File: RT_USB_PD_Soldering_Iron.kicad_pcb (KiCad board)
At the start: 4 copper layers, 75 x 11 mm, 62 parts, among them J1 USB4105-GF-A, J2 35RASMT4BHNTRX, J3 Conn_02x03_Odd_Even, SW1 SW_Push, SW2 SW_Push, U1 SPX3819M5-L-3-3, U2 BMI270, U3 DRTR5V0U4S-7, U5 STM32G431Kxxx, U6 TPS25982ONRGET, U7 OPA376AIDCKR, U8 STTS22H, Y1 NX2016SA-24MHZ-EXS00A-CS10820

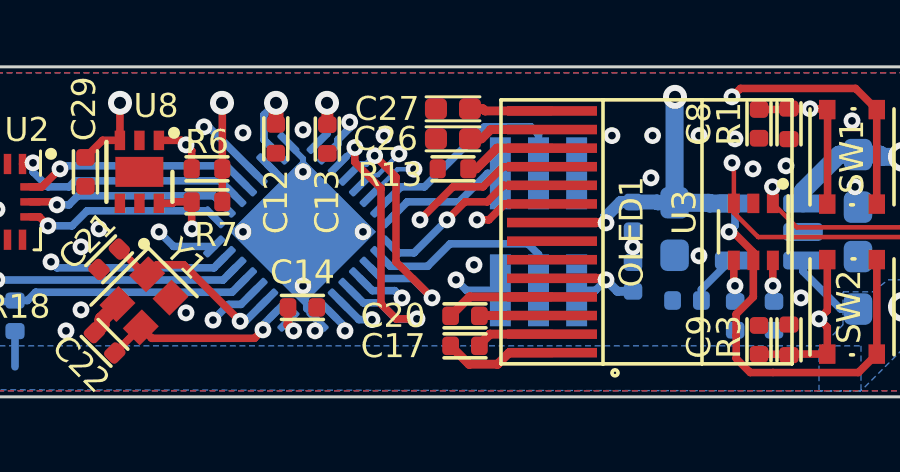
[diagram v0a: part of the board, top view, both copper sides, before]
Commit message: slight change in capacitor layout
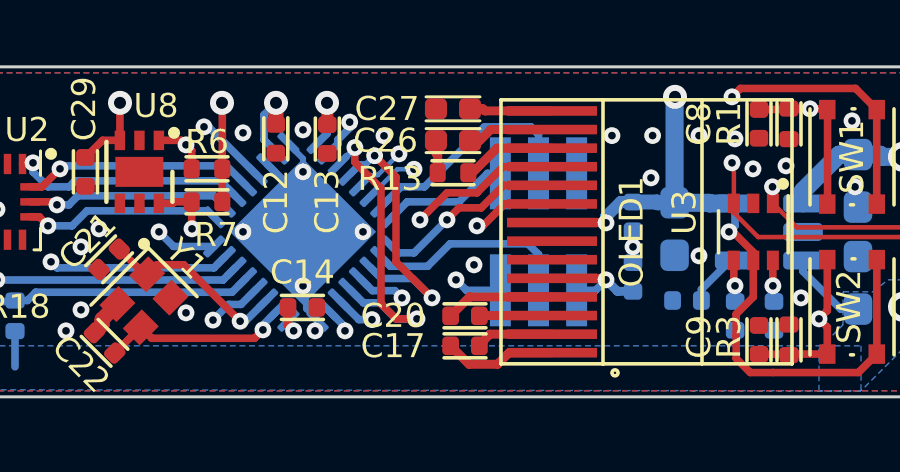
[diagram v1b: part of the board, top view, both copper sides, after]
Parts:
- moved R13 0.13 mm to (152.2, 123.0)
- moved C26 0.06 mm to (152.2, 122.0)
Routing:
- net GND: track 17.2 -> 18.3 mm
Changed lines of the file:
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@@
   )
   (module "local:C_0402_1005Metric_Pad0.74x0.62mm_HandSolder" (layer "F.Cu")
-    (at 152.2 121.9)
+    (at 152.2 121.958771)
     (descr "Capacitor SMD 0402 (1005 Metric), square (rectangular) end terminal, IPC_7351 nominal with elongated pad for handsoldering. (Body size source: IPC-SM-782 page 76, https://www.pcb-3d.com/wordpress/wp-content/uploads/ipc-sm-782a_amendment_1_and_2.pdf), generated with kicad-footprint-generator")
     (tags "capacitor handsolder")
@@
   )
   (module "local:R_0402_1005Metric" (layer "F.Cu")
-    (at 152.2 122.9)
+    (at 152.2 123.029328)
     (descr "Resistor SMD 0402 (1005 Metric), square (rectangular) end terminal, IPC_7351 nominal, (Body size source: IPC-SM-782 page 72, https://www.pcb-3d.com/wordpress/wp-content/uploads/ipc-sm-782a_amendment_1_and_2.pdf), generated with kicad-footprint-generator")
     (tags "resistor")
@@
   (segment (start 127.6 123.8) (end 127.2 124.2) (width 0.254) (layer "F.Cu") (net 15))
   (segment (start 126.85 124.95) (end 126.325 124.95) (width 0.254) (layer "F.Cu") (net 15))
-  (segment (start 153.15 121.9) (end 153.46 121.59) (width 0.3) (layer "F.Cu") (net 16))
-  (segment (start 153.46 121.59) (end 155.5 121.59) (width 0.3) (layer "F.Cu") (net 16))
-  (segment (start 153.15 121.9) (end 152.7675 121.9) (width 0.3) (layer "F.Cu") (net 16))
+  (segment (start 155.5 121.59) (end 153.46 121.59) (width 0.3) (layer "F.Cu") (net 16))
+  (segment (start 153.091229 121.958771) (end 152.7675 121.958771) (width 0.3) (layer "F.Cu") (net 16))
+  (segment (start 153.46 121.59) (end 153.091229 121.958771) (width 0.3) (layer "F.Cu") (net 16))
   (segment (start 153.2 120.9) (end 152.7675 120.9) (width 0.3) (layer "F.Cu") (net 17))
   (segment (start 155.5 120.97) (end 153.27 120.97) (width 0.3) (layer "F.Cu") (net 17))
@@
   (segment (start 131.3 120.9) (end 106.55 120.9) (width 0.4) (layer "In1.Cu") (net 22))
   (segment (start 105.35 120.9) (end 106.55 120.9) (width 0.4) (layer "B.Cu") (net 22))
-  (segment (start 152.98 122.9) (end 153.67 122.21) (width 0.3) (layer "F.Cu") (net 23))
+  (segment (start 152.850672 123.029328) (end 153.67 122.21) (width 0.3) (layer "F.Cu") (net 23))
   (segment (start 153.67 122.21) (end 155.5 122.21) (width 0.3) (layer "F.Cu") (net 23))
-  (segment (start 152.71 122.9) (end 152.98 122.9) (width 0.3) (layer "F.Cu") (net 23))
+  (segment (start 152.71 123.029328) (end 152.850672 123.029328) (width 0.3) (layer "F.Cu") (net 23))
   (segment (start 161.590953 125.954086) (end 161.445914 125.954086) (width 0.254) (layer "B.Cu") (net 24))
   (segment (start 161.445914 125.954086) (end 160.47954 126.92046) (width 0.254) (layer "B.Cu") (net 24))
@@
   (segment (start 125.85 123.95) (end 126.325 123.95) (width 0.254) (layer "F.Cu") (net 25))
   (segment (start 136.0875 124) (end 134.936877 124) (width 0.254) (layer "F.Cu") (net 25))
+  (segment (start 151.6325 121.958771) (end 151.6325 122.3825) (width 0.3) (layer "F.Cu") (net 25))
   (segment (start 126.325 124.45) (end 125.45 124.45) (width 0.254) (layer "F.Cu") (net 25))
+  (segment (start 151.6325 122.3825) (end 151.69 122.44) (width 0.3) (layer "F.Cu") (net 25))
   (segment (start 140.24659 128.360589) (end 140.5 128.107179) (width 0.5) (layer "F.Cu") (net 25))
   (segment (start 124.65 126.880201) (end 125.3 126.230201) (width 0.254) (layer "F.Cu") (net 25))
@@
   (segment (start 125.5 124.3) (end 125.85 123.95) (width 0.254) (layer "F.Cu") (net 25))
   (segment (start 140.5 127.922183) (end 141.016117 127.406066) (width 0.5) (layer "F.Cu") (net 25))
+  (segment (start 151.69 122.44) (end 151.69 123.029328) (width 0.3) (layer "F.Cu") (net 25))
   (segment (start 135.8 124.5) (end 135.7 124.6) (width 0.254) (layer "F.Cu") (net 25))
   (via (at 135.75 128.3) (size 0.56) (drill 0.254) (layers "F.Cu" "B.Cu") (remove_unused_layers) (keep_end_layers) (net 25))
@@
   (segment (start 147.2 122.560482) (end 147.2 123) (width 0.2032) (layer "B.Cu") (net 25))
   (segment (start 146.713864 122.03899) (end 146.713864 122.074346) (width 0.2032) (layer "B.Cu") (net 25))
-  (segment (start 153.890817 123.45) (end 153.340817 124) (width 0.254) (layer "F.Cu") (net 26))
+  (segment (start 153.890817 123.45) (end 153.140817 124.2) (width 0.254) (layer "F.Cu") (net 26))
   (segment (start 143.49 122.29) (end 143.3 122.1) (width 0.254) (layer "F.Cu") (net 26))
   (segment (start 155.5 123.45) (end 153.890817 123.45) (width 0.254) (layer "F.Cu") (net 26))
+  (segment (start 152.4 124.2) (end 152 124.6) (width 0.254) (layer "F.Cu") (net 26))
   (segment (start 142.397498 121.95) (end 143.15 121.95) (width 0.254) (layer "F.Cu") (net 26))
-  (segment (start 153.340817 124) (end 152.6 124) (width 0.254) (layer "F.Cu") (net 26))
   (segment (start 143.15 121.95) (end 143.3 122.1) (width 0.254) (layer "F.Cu") (net 26))
-  (segment (start 152.6 124) (end 152 124.6) (width 0.254) (layer "F.Cu") (net 26))
   (segment (start 143.49 122.9) (end 143.49 122.29) (width 0.254) (layer "F.Cu") (net 26))
+  (segment (start 153.140817 124.2) (end 152.4 124.2) (width 0.254) (layer "F.Cu") (net 26))
   (via (at 152 124.6) (size 0.56) (drill 0.254) (layers "F.Cu" "B.Cu") (remove_unused_layers) (keep_end_layers) (net 26))
   (via (at 143.3 122.1) (size 0.56) (drill 0.254) (layers "F.Cu" "B.Cu") (remove_unused_layers) (keep_end_layers) (net 26))
@@
   (segment (start 142.85 124.05) (end 142.9 124) (width 0.254) (layer "F.Cu") (net 27))
   (segment (start 155.5 122.83) (end 153.87 122.83) (width 0.254) (layer "F.Cu") (net 27))
-  (segment (start 153.87 122.83) (end 153.20059 123.49941) (width 0.254) (layer "F.Cu") (net 27))
-  (segment (start 153.20059 123.49941) (end 152.20059 123.49941) (width 0.254) (layer "F.Cu") (net 27))
-  (segment (start 152.20059 123.49941) (end 151.1 124.6) (width 0.254) (layer "F.Cu") (net 27))
+  (segment (start 153.87 122.83) (end 153 123.7) (width 0.254) (layer "F.Cu") (net 27))
   (segment (start 142.9 124) (end 143.49 124) (width 0.254) (layer "F.Cu") (net 27))
   (segment (start 143.49 124.89) (end 143.5 124.9) (width 0.254) (layer "F.Cu") (net 27))
+  (segment (start 153 123.7) (end 152 123.7) (width 0.254) (layer "F.Cu") (net 27))
   (segment (start 143.49 124) (end 143.49 124.89) (width 0.254) (layer "F.Cu") (net 27))
+  (segment (start 152 123.7) (end 151.1 124.6) (width 0.254) (layer "F.Cu") (net 27))
   (segment (start 142.397498 124.05) (end 142.85 124.05) (width 0.254) (layer "F.Cu") (net 27))
   (via (at 151.1 124.6) (size 0.56) (drill 0.254) (layers "F.Cu" "B.Cu") (remove_unused_layers) (keep_end_layers) (net 27))
@@
   (segment (start 139.395979 124.1) (end 139 124.1) (width 0.254) (layer "B.Cu") (net 37))
   (segment (start 144.232233 123.8) (end 139.695979 123.8) (width 0.254) (layer "B.Cu") (net 37))
-  (segment (start 153.925979 124.07) (end 153.395979 124.6) (width 0.254) (layer "F.Cu") (net 38))
-  (segment (start 153.395979 124.6) (end 153 124.6) (width 0.254) (layer "F.Cu") (net 38))
   (segment (start 155.5 124.07) (end 153.925979 124.07) (width 0.254) (layer "F.Cu") (net 38))
+  (segment (start 153.925979 124.07) (end 153.195979 124.8) (width 0.254) (layer "F.Cu") (net 38))
+  (segment (start 153.195979 124.8) (end 153 124.8) (width 0.254) (layer "F.Cu") (net 38))
+  (via (at 153 124.8) (size 0.56) (drill 0.254) (layers "F.Cu" "B.Cu") (net 38))
   (via (at 150.5 127.2) (size 0.56) (drill 0.254) (layers "F.Cu" "B.Cu") (remove_unused_layers) (keep_end_layers) (net 38))
-  (via (at 153 124.6) (size 0.56) (drill 0.254) (layers "F.Cu" "B.Cu") (remove_unused_layers) (keep_end_layers) (net 38))
-  (segment (start 153 124.7) (end 153 124.6) (width 0.254) (layer "In2.Cu") (net 38))
-  (segment (start 150.5 127.2) (end 153 124.7) (width 0.254) (layer "In2.Cu") (net 38))
+  (segment (start 150.5 127.2) (end 152.9 124.8) (width 0.254) (layer "In2.Cu") (net 38))
+  (segment (start 152.9 124.8) (end 153 124.8) (width 0.254) (layer "In2.Cu") (net 38))
   (segment (start 149.51378 126.960227) (end 150.260227 126.960227) (width 0.254) (layer "B.Cu") (net 38))
   (segment (start 149.100349 126.546796) (end 149.51378 126.960227) (width 0.254) (layer "B.Cu") (net 38))

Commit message: First revision 0.1
Rev 0.1 untested unverified.
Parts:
- removed C21, C22: 6.8p 50v, local:C_0402_1005Metric
- removed C29: 0.1uF 50v, local:C_0402_1005Metric
- removed U8: STTS22H, local:DFN-6-1EP_2x2mm_P0.65mm_EP1x1.6mm
- removed Y1: NX2016SA-24MHZ-EXS00A-CS10820, local:Crystal_SMD_2016-4Pin_2.0x1.6mm
- added C10: 220pF 50v, Capacitor_SMD:C_0402_1005Metric, B.Cu at (164.8, 127.1)
- added C11: 220pF 50v, Capacitor_SMD:C_0402_1005Metric, B.Cu at (162.4, 124.4)
- added TH1: Thermistor_NTC, Resistor_SMD:R_0402_1005Metric, F.Cu at (108.0, 121.2)
- added U4: FUSB302BMPX, Package_DFN_QFN:WQFN-14-1EP_2.5x2.5mm_P0.5mm_EP1.45x1.45mm, B.Cu at (162.5, 126.9)
- C4: value 1u 50v -> 10uF 35v; footprint local:C_0402_1005Metric -> Capacitor_SMD:C_0603_1608Metric_Pad1.05x0.95mm_HandSolder
- C6: value 220pF 50v -> 1u 50v; footprint local:C_0402_1005Metric -> Capacitor_SMD:C_0402_1005Metric
- C7: value 220pF 50v -> 0.1uF 50v; footprint local:C_0402_1005Metric -> Capacitor_SMD:C_0402_1005Metric
- R2: value 75K 0.5% -> 10K 1%; footprint local:R_0402_1005Metric -> Resistor_SMD:R_0402_1005Metric; moved to F.Cu
- R4: value 12K 0.5% -> 2.2K 5%; footprint local:R_0402_1005Metric -> Resistor_SMD:R_0402_1005Metric; moved to F.Cu
- U3: value DRTR5V0U4S-7 -> ECMF02-AMX6; footprint local:SOT-363_SC-70-6 -> Package_DFN_QFN:ST_UQFN-6L_1.5x1.7mm_Pitch0.5mm
- moved C1 37.1 mm to (128.6, 127.8)
- moved C6 18.9 mm to (144.0, 127.8)
- moved R7 17.2 mm to (161.2, 123.4), turned to -90 degrees
- moved R6 16.2 mm to (160.2, 123.4), turned to -90 degrees
- moved R4 15.9 mm to (149.6, 121.4)
- moved R2 6.40 mm to (144.0, 127.8)
- moved C4 5.80 mm to (130.6, 127.8)
- moved U3 3.59 mm to (165.8, 125.0), turned to 180 degrees
- moved U1 3.02 mm to (161.6, 122.2)
- moved C3 2.92 mm to (160.4, 124.4), turned to 0 degrees
- moved C2 2.92 mm to (158.5, 122.2)
- moved C7 2.54 mm to (159.2, 127.0), turned to -90 degrees
- moved C8 2.20 mm to (160.2, 121.4)
- moved R1 2.18 mm to (161.2, 121.4)
- moved C9 2.17 mm to (160.2, 128.6)
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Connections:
- net /INT0 renamed /BMI270_INT0
- net Net-(J1-PadA8) renamed no_connect_54
- net Net-(J1-PadB8) renamed no_connect_55
- net Net-(OLED1-Pad6) renamed no_connect_56
- net Net-(U2-Pad10) renamed no_connect_57
- net Net-(U2-Pad11) renamed no_connect_58
- net Net-(U2-Pad2) renamed no_connect_59
- net Net-(U2-Pad3) renamed no_connect_60
- net Net-(U2-Pad9) renamed no_connect_61
- C4 pad 1: GND -> IN
- C4 pad 2: /PVD_IN -> GND
- C6 pad 2: /CC1 -> /BOARD_TEMP
- C7 pad 2: /CC2 -> +3V3
- J1 pad A6: /USB_P -> /USB_P_IN
- J1 pad A7: /USB_N -> /USB_N_IN
- J1 pad B6: /USB_P -> /USB_P_IN
- J1 pad B7: /USB_N -> /USB_N_IN
- R2 pad 1: IN -> +3V3
- R2 pad 2: /PVD_IN -> /BOARD_TEMP
- R4 pad 1: /PVD_IN -> +3V3
- R4 pad 2: GND -> /FUSB_INT_N
- U3 pad 1: /USB_P -> /USB_N_IN
- U3 pad 2: GND -> /USB_P_IN
- U3 pad 3: /USB_N -> GND
- U3 pad 4: /CC2 -> GND
- U3 pad 5: +3V3 -> /USB_P
- U3 pad 6: /CC1 -> /USB_N
- U5 pad 19: /CC1 -> /FUSB_INT_N
- U5 pad 2: /OSC_IN -> Net-(U5-Pad2)
- U5 pad 20: /CC2 -> Net-(U5-Pad20)
- U5 pad 27: /CC2 -> Net-(U5-Pad27)
- U5 pad 29: /CC1 -> Net-(U5-Pad29)
- U5 pad 3: /OSC_OUT -> Net-(U5-Pad3)
- U5 pad 5: /PVD_IN -> /BOARD_TEMP
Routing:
- net /BOARD_TEMP: track 0.00 -> 40.5 mm, vias 0 -> 2
- net /CC1: track 32.5 -> 7.39 mm, vias 4 -> 1
- net /CC2: track 31.6 -> 11.3 mm, vias 4 -> 1
- net /FUSB_INT_N: track 0.00 -> 16.4 mm, vias 0 -> 2
- net /PVD_IN: track 10.4 -> 0.00 mm
- net +3V3: track 97.0 -> 88.8 mm, vias 11 -> 9
- net IN: track 31.9 -> 39.2 mm
- net /OSC_IN: track 6.41 -> 0.00 mm, vias 1 -> 0
- net /OSC_OUT: track 6.40 -> 0.00 mm, vias 1 -> 0
- net /USB_P: track 23.2 -> 17.5 mm
- net /USB_N: track 23.4 -> 18.3 mm
- net /USB_P_IN: track 0.00 -> 4.57 mm
- net /BTN1: track 22.7 -> 18.6 mm
- net /USB_N_IN: track 0.00 -> 3.58 mm
- net /BTN2: track 22.3 -> 18.8 mm
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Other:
- board text added: "Stephanie's RTx PD IRON Rev 0.1"

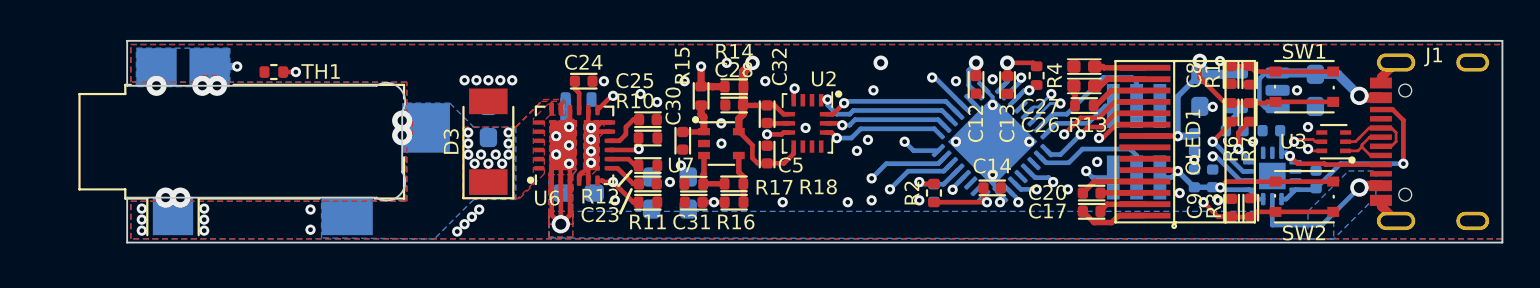
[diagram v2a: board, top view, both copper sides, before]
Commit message: Add mounting holes, change diode
added mounting holes and changed the diode to a much smaller part.
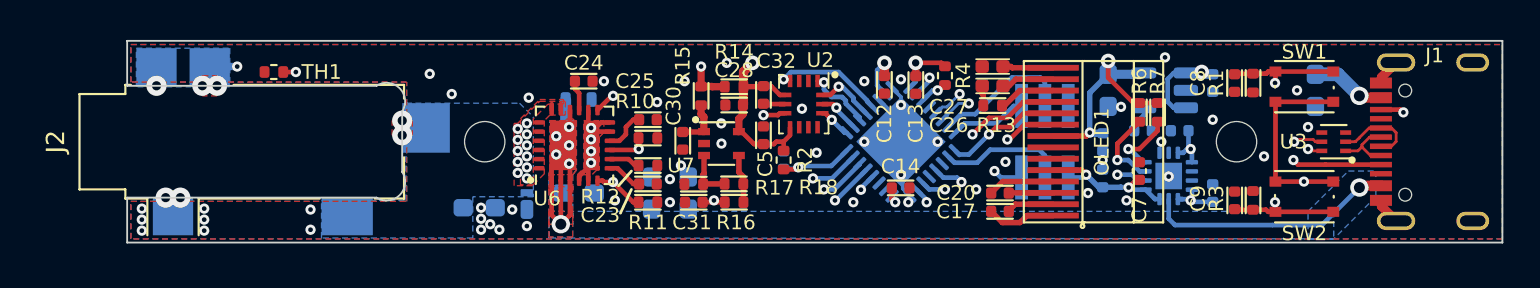
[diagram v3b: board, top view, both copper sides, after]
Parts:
- added C21: 1u 50v, Capacitor_SMD:C_0402_1005Metric, B.Cu at (159.2, 121.8)
- added H1: MountingHole, MountingHole:MountingHole_2.2mm_M2_ISO7380, F.Cu at (160.5, 125.0)
- added H2: MountingHole, MountingHole:MountingHole_2.2mm_M2_ISO7380, F.Cu at (119.5, 125.0)
- C7: moved to F.Cu
- D3: footprint local:D_SOD-128 -> local:X3-WLB1608-2; moved to B.Cu
- moved C6 8.40 mm to (135.8, 126.0), turned to -90 degrees
- moved R2 8.40 mm to (135.8, 126.0), turned to -90 degrees
- moved C10 5.69 mm to (159.2, 127.8)
- moved U4 5.65 mm to (156.8, 126.9)
- moved C11 5.00 mm to (157.4, 124.4)
- moved C12 5.00 mm to (141.3, 121.9)
- moved C13 5.00 mm to (143.0, 121.9)
- moved C14 5.00 mm to (142.2, 127.5)
- moved C17 5.00 mm to (147.6, 128.8)
- moved C18 5.00 mm to (153.2, 125.0)
- moved C19 5.00 mm to (153.2, 127.0)
- moved C2 5.00 mm to (153.5, 122.2)
- moved C20 5.00 mm to (147.6, 127.8)
- moved C26 5.00 mm to (147.2, 122.0)
- moved C27 5.00 mm to (147.2, 120.9)
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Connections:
- U5 pad 13: /HEAT_ON -> /BMI270_INT0
- U5 pad 5: /BOARD_TEMP -> /TEMP_SENS
- U5 pad 6: /TEMP_SENS -> /HEAT_ON
- U5 pad 8: /BMI270_INT0 -> /BOARD_TEMP
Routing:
- net IN: track 39.2 -> 53.7 mm, vias 8 -> 9
- net /HEAT_ON: track 26.8 -> 16.9 mm, vias 3 -> 2
- net /BTN1: track 18.6 -> 26.3 mm
- net /BTN2: track 18.8 -> 26.4 mm
- net /CC2: track 11.3 -> 17.7 mm, vias 1 -> 2
- net /CC1: track 7.39 -> 13.6 mm, vias 1 -> 2
- net /BOARD_TEMP: track 40.5 -> 34.9 mm
- net /VSENSE: track 20.0 -> 15.0 mm
- net /USB_N: track 18.3 -> 23.3 mm
- net /USB_P: track 17.5 -> 22.4 mm
- net /TEMP_SENS: track 15.0 -> 10.3 mm
- net /SPI1_SCK: track 6.79 -> 2.24 mm
- net /SPI1_NSS: track 6.25 -> 1.77 mm
- net /SPI1_MOSI: track 7.75 -> 3.27 mm
- net /SPI1_MISO: track 7.91 -> 3.57 mm
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
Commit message: Power trace changes, pin changes
updated the power traces for better current return path. Connected PG from the high side switch.
Lots of pin changes for better layout.
re-annotated schematic
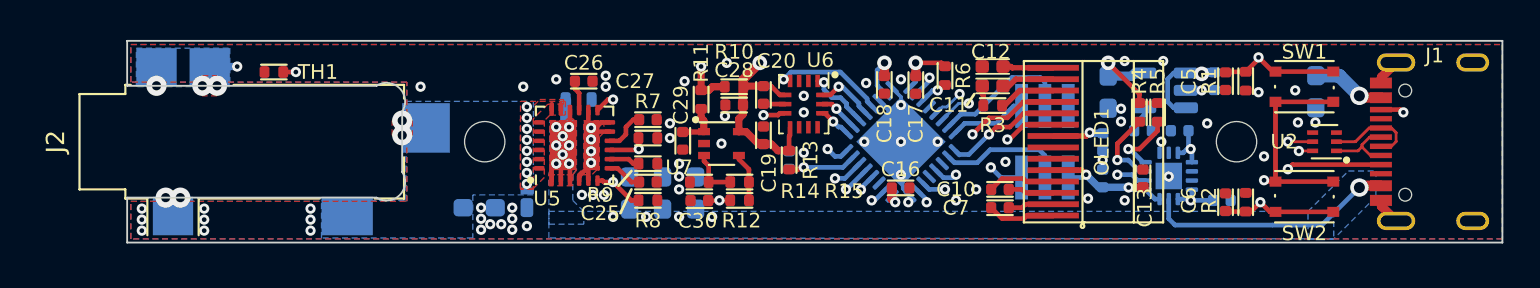
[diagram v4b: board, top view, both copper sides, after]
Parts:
- C13: renamed from C7; footprint Capacitor_SMD:C_0402_1005Metric -> local:C_0402_1005Metric
- C14: renamed from C11; footprint Capacitor_SMD:C_0402_1005Metric -> local:C_0402_1005Metric
- C15: renamed from C10; footprint Capacitor_SMD:C_0402_1005Metric -> local:C_0402_1005Metric
- C2: renamed from C21; footprint Capacitor_SMD:C_0402_1005Metric -> local:C_0402_1005Metric
- C31: renamed from C6; footprint Capacitor_SMD:C_0402_1005Metric -> local:C_0402_1005Metric
- R13: renamed from R2; footprint Resistor_SMD:R_0402_1005Metric -> local:R_0402_1005Metric
- R6: renamed from R4; footprint Resistor_SMD:R_0402_1005Metric -> local:R_0402_1005Metric
- TH1: footprint Resistor_SMD:R_0402_1005Metric -> local:R_0402_1005Metric
- moved C24 2.80 mm to (127.4, 127.8), turned to 90 degrees
- moved C15 0.64 mm to (159.7, 128.2), turned to 180 degrees
- moved C22 0.60 mm to (129.2, 127.8)
- moved C6 0.51 mm to (159.9, 128.3)
- moved C5 0.51 mm to (159.9, 121.7)
- moved U2 0.50 mm to (165.3, 125.0)
- moved C13 0.45 mm to (155.4, 127.0)
- moved R2 0.41 mm to (161.0, 128.3)
- moved R1 0.41 mm to (161.0, 121.7)
- moved C23 0.40 mm to (131.0, 127.8)
- moved R15 0.32 mm to (133.4, 127.2)
- moved R14 0.32 mm to (131.2, 127.2)
- moved R12 0.32 mm to (133.4, 128.2)
- moved C30 0.32 mm to (131.2, 128.2)
- moved C31 0.30 mm to (136.1, 126.0)
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- renumbered C33 to C1, C20 to C10, C26 to C11, C27 to C12, C14 to C16, C13 to C17, C12 to C18, C5 to C19, C32 to C20, C16 to C21, C1 to C22, C4 to C23, C15 to C24, C23 to C25, C24 to C26, C25 to C27, C30 to C29, C31 to C30, C2 to C4, C8 to C5, C9 to C6, C17 to C7, C18 to C8, C19 to C9, D3 to D1, R14 to R10, R15 to R11, R16 to R12, R17 to R14, R18 to R15, R3 to R2, R13 to R3, R6 to R4, R7 to R5, R10 to R7, R11 to R8, R12 to R9, U3 to U2, U4 to U3, U5 to U4, U6 to U5, U2 to U6
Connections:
- J1 pad A8: no_connect_54 -> no_connect_53
- J1 pad B8: no_connect_55 -> no_connect_54
- OLED1 pad 6: no_connect_56 -> no_connect_55
- U4 pad 2: Net-(U5-Pad2) -> /TEMP_SENS
- U4 pad 5: /TEMP_SENS -> /HEAT_ON
- U4 pad 6: /HEAT_ON -> /VSENSE
- U4 pad 7: /VSENSE -> /BOARD_TEMP
- U4 pad 8: /BOARD_TEMP -> /HEATER_PG
- U6 pad 10: no_connect_57 -> no_connect_56
- U6 pad 11: no_connect_58 -> no_connect_57
- U6 pad 2: no_connect_59 -> no_connect_58
- U6 pad 3: no_connect_60 -> no_connect_59
- U6 pad 9: no_connect_61 -> no_connect_60
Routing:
- net /HEATER_PG: track 1.17 -> 15.2 mm, vias 1 -> 2
- net IN: track 53.7 -> 45.7 mm, vias 9 -> 15
- net +3V3: track 89.9 -> 88.7 mm
- net /HEAT_ON: track 16.9 -> 17.6 mm
- net /BOARD_TEMP: track 34.9 -> 34.3 mm
- net /USB_P: track 22.4 -> 21.8 mm
- net /USB_N_IN: track 3.58 -> 4.08 mm
- net /USB_P_IN: track 4.57 -> 5.07 mm
- net GND: vias 58 -> 72
- net /HEATER: vias 13 -> 10
